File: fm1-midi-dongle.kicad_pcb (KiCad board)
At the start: 4 copper layers, 20 x 37.7 mm, 28 parts, among them J1 TYPE-C 24P-GTJB 040, J2 TYPE-C-31-M-12, J3 PJ-320D, J4 PJ-320D, U1 CH32X035G8U6, U2 XC6206P332MR, U3 SY6280AAC, U4 H11L1SM

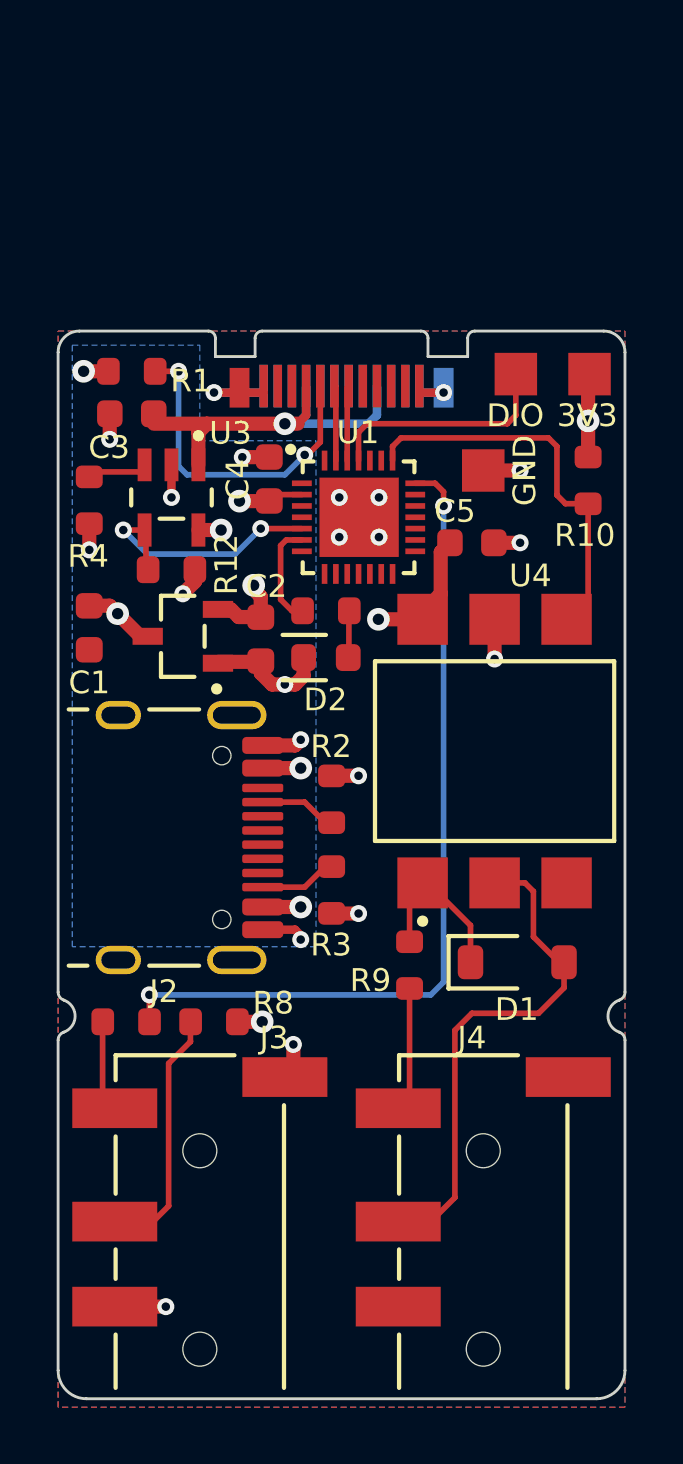
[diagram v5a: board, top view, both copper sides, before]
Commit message: Add hardware MIDI THRU: U5 SPDT switch selects OUT jack source
SN74LVC1G3157DCKR (LCSC C38663) in front of R7/J3 tip: S low = MIDI_RX
(opto output, hardware THRU), S high = MIDI_TX. S = OUT_SEL = PB9 with
R13 100k pull-down so THRU is the default with a blank or resetting MCU.

Layout: U5 between MCU and opto, C5 and R13 moved, TP3 (GND) moved to
the pocket above the jacks. ERC 0, DRC only the 6 known J1 edge items.
BOM, DESIGN.md and renders updated; SC-70-6 STEP vendored.

Co-Authored-By: Claude Opus 5.5 <noreply@anthropic.com>
Claude-Session: https://claude.ai/code/session_01Dtfv3zuhZTs975LiSXznFQ
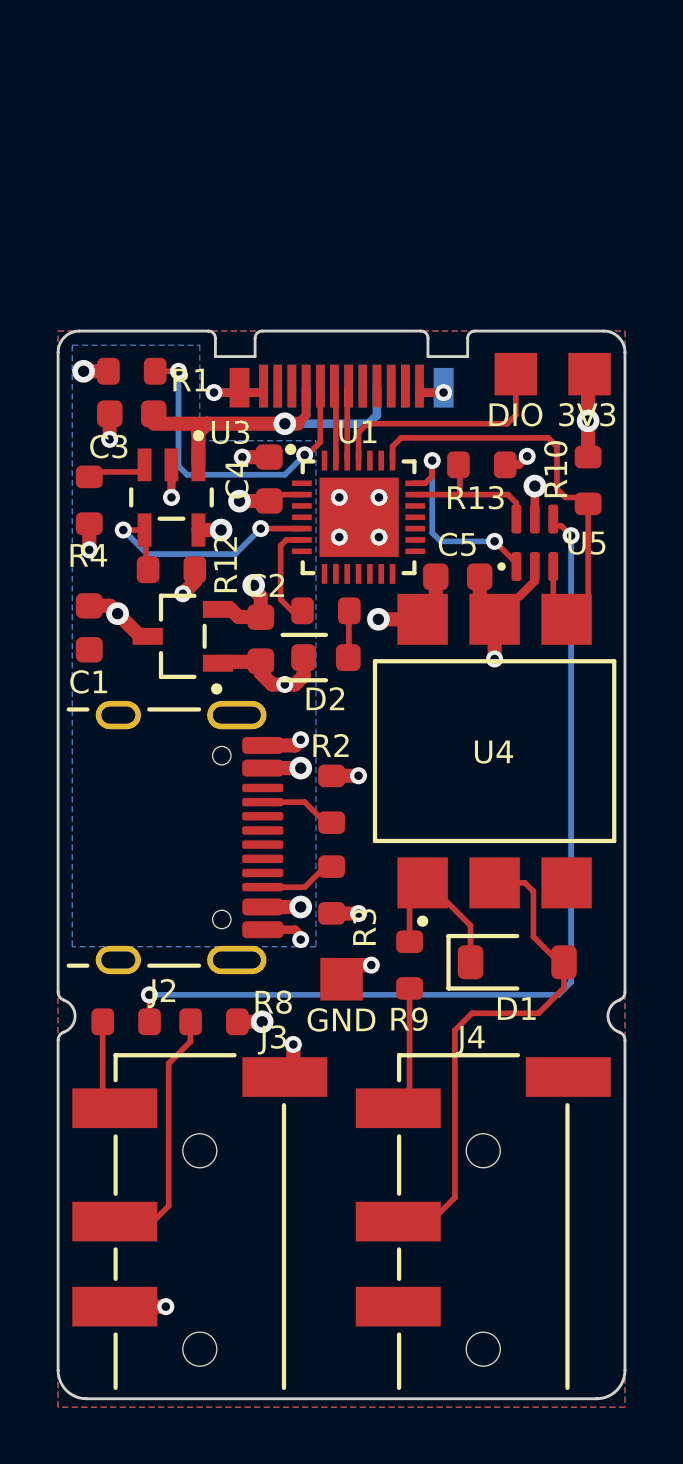
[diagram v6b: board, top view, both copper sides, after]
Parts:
- added R13: 100k, R_0603_1608Metric, F.Cu at (4.95, 2.75)
- added U5: SN74LVC1G3157, SOT-363_SC-70-6, F.Cu at (6.82, 5.50)
- moved TP3 18.6 mm to (0.00, 20.9)
- moved C5 1.30 mm to (4.10, 6.70)
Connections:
- R7 pad 1: /MIDI_TX -> /MIDI_OUT_DATA
- U1 pad 20: (no net) -> /OUT_SEL
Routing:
- net /MIDI_OUT_DATA: track 0.00 -> 32.5 mm, vias 0 -> 2
- net /MIDI_TX: track 29.9 -> 7.08 mm
- net /OUT_SEL: track 0.00 -> 4.57 mm
- net +3V3: track 13.1 -> 11.8 mm, vias 5 -> 6
- net GND: track 26.1 -> 27.0 mm

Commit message: v5: USB-A host port on the bottom face, schematic cleanup, hand-routed
- J1 = USB-A receptacle 911-321B2028S10100 (LCSC C42474) on B.Cu, mouth 0.8 mm
  past the top edge; board still 20 x 37.7 mm. Plug, R1 and CC_FM1 removed,
  VBUS_HOST, C3 now 10 uF (C96446) host-port bulk.
- Schematic: power/ground as KiCad power symbols, no overlapping symbols or
  texts (generator checks it), clean symbols for SY6280, 3157, USB-A, PJ-320D.
- THRU switch inputs swapped (B2 = MIDI_RX, B1 = MIDI_TX) and R13 is now a
  pull-up: THRU still default; firmware drives PB9 low for MCU MIDI.
- Floorplan + hand-written routing (tools/route.py): DRC 0 unconnected, house
  style clean, 0 loops. One track_width neck at U1 VDD (0.4 mm pitch).
- TP3 (GND) moved to the top-left corner; opto block 2.1 mm lower.
- Renders, BOM and DESIGN.md updated.

Co-Authored-By: Claude Opus 5.5 <noreply@anthropic.com>
Claude-Session: https://claude.ai/code/session_01Dtfv3zuhZTs975LiSXznFQ
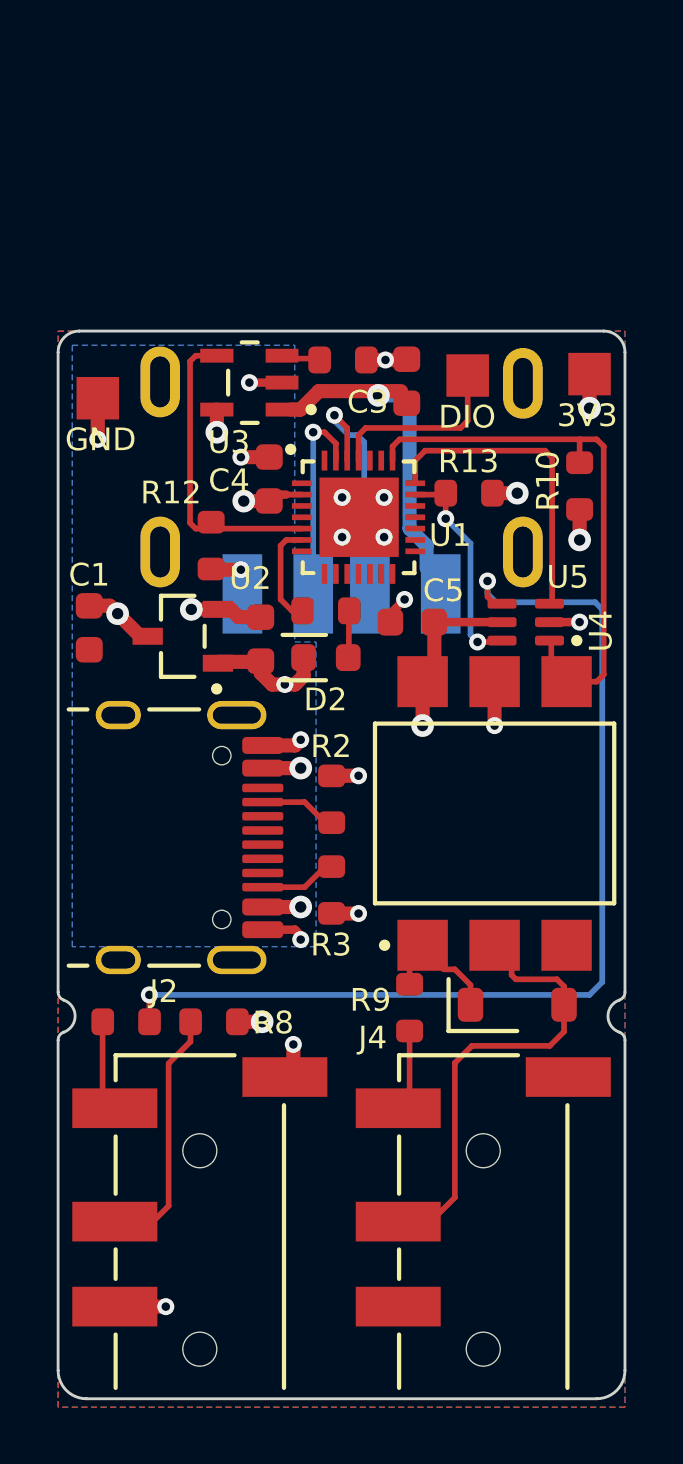
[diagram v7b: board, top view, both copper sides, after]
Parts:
- removed R1: 56k, R_0603_1608Metric
- C3: value 1u -> 10u
- J1: value TYPE-C 24P-GTJB 040 -> 911-321B2028S10100; footprint USB-C-SMD_TYPE-C-24P-GTJB-040 -> USB-A-SMD_911-321B2028S10100; moved to B.Cu
- moved TP3 22.2 mm to (-8.60, 0.40)
- moved R4 10.2 mm to (0.05, -0.95), turned to 0 degrees
- moved C3 9.77 mm to (2.30, -0.20), turned to 90 degrees
- moved U3 4.90 mm to (-3.25, -0.15), turned to 90 degrees
- moved J1 3.56 mm to (0.00, 3.56), turned to 0 degrees
- moved U5 2.82 mm to (6.50, 8.30), turned to 180 degrees
- moved C5 2.26 mm to (2.50, 8.30), turned to 180 degrees
- moved U4 2.20 mm to (5.40, 15.1)
- moved TP2 1.70 mm to (4.45, -0.40)
- moved R12 1.64 mm to (-4.60, 5.60), turned to -90 degrees
- moved D1 1.50 mm to (6.20, 21.8)
- moved R9 1.50 mm to (2.40, 21.9)
- moved R13 1.10 mm to (4.50, 3.75), turned to 180 degrees
- moved R10 0.36 mm to (8.40, 3.50), turned to 90 degrees
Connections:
- C3 pad 1: /VBUS_FM1 -> VBUS_HOST
- R13 pad 1: /OUT_SEL -> +3V3
- R13 pad 2: GND -> /OUT_SEL
- U3 pad 1: /VBUS_FM1 -> VBUS_HOST
- U5 pad 1: /MIDI_TX -> /MIDI_RX
- U5 pad 3: /MIDI_RX -> /MIDI_TX
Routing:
- net /VBUS_FM1: track 13.9 -> 0.00 mm, vias 1 -> 0
- net /CC_FM1: track 11.7 -> 0.00 mm, vias 2 -> 0
- net VBUS_HOST: track 0.00 -> 11.4 mm, vias 0 -> 1
- net GND: track 27.0 -> 20.5 mm, vias 21 -> 19
- net /USB_DM: track 2.60 -> 7.80 mm, vias 0 -> 1
- net /MIDI_RX: track 13.4 -> 18.2 mm
- net /MIDI_TX: track 7.08 -> 11.0 mm, vias 2 -> 0
- net /USB_DP: track 2.60 -> 6.37 mm, vias 0 -> 1
- net /MIDI_IN_RING: track 18.2 -> 14.6 mm
- net /MIDI_OUT_DATA: track 32.5 -> 35.9 mm
- net /OUT_SEL: track 4.57 -> 7.34 mm, vias 0 -> 2
- net /OPTO_A: track 4.28 -> 1.98 mm
- net /SDI_DIO: track 8.25 -> 5.96 mm
- net /VBUS_EN: track 8.77 -> 10.6 mm, vias 2 -> 0
- net /MIDI_IN_TIP: track 4.22 -> 2.57 mm
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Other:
- outline, holes or cut-outs redrawn
- board text added: "USB HOST"
- board text added: "v5 2026-10"
- board text removed: "v4 2026-10"

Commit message: v6: flat-slab layout, hand-routed, slab case
Owner rejected the v5 S-profile case (can't lie flat on a desk) and chose a
re-placed board in a uniform 12.2 mm slab.

- Board (still 20 x 37.7 mm): tall parts on top (USB-A J1 now on top, USB-C
  J2 on the right edge, jacks, opto, THRU switch, LED); parts <= 1.3 mm on
  the bottom (MCU, LDO, SY6280, caps, SDI pads).
- Pins: VBUS_EN -> PA3 (pin 8), LED -> PB12 (pin 23); U5 B1 = RX, B2 = TX,
  R13 back to a pull-down (PB9 HIGH = MCU TX, default hardware THRU).
- Routing (tools/route.py, hand-written polylines): +5V_IN as an island in
  In2; DRC 0 unconnected / 0 clearance, 0 loops, style clean. Open for
  owner sign-off: VDD 0.2 mm neck, one 0.6/0.3 +5V via, 0.8 mm designators.
- tools/silk.py is face-aware (outlines, designators and labels on each
  part's own face, back text mirrored); per-face net renders.
- case/: rounded slab 22.8 x 41.0 x 12.2 mm, flat top and bottom, snap fit,
  USB-A / USB-C dishes, flush jacks, LED light pipe; check_fit 0 collisions.
- DESIGN.md v6 section and firmware pin changes; BOM notes.

Co-Authored-By: Claude Opus 5.5 <noreply@anthropic.com>
Claude-Session: https://claude.ai/code/session_01Dtfv3zuhZTs975LiSXznFQ
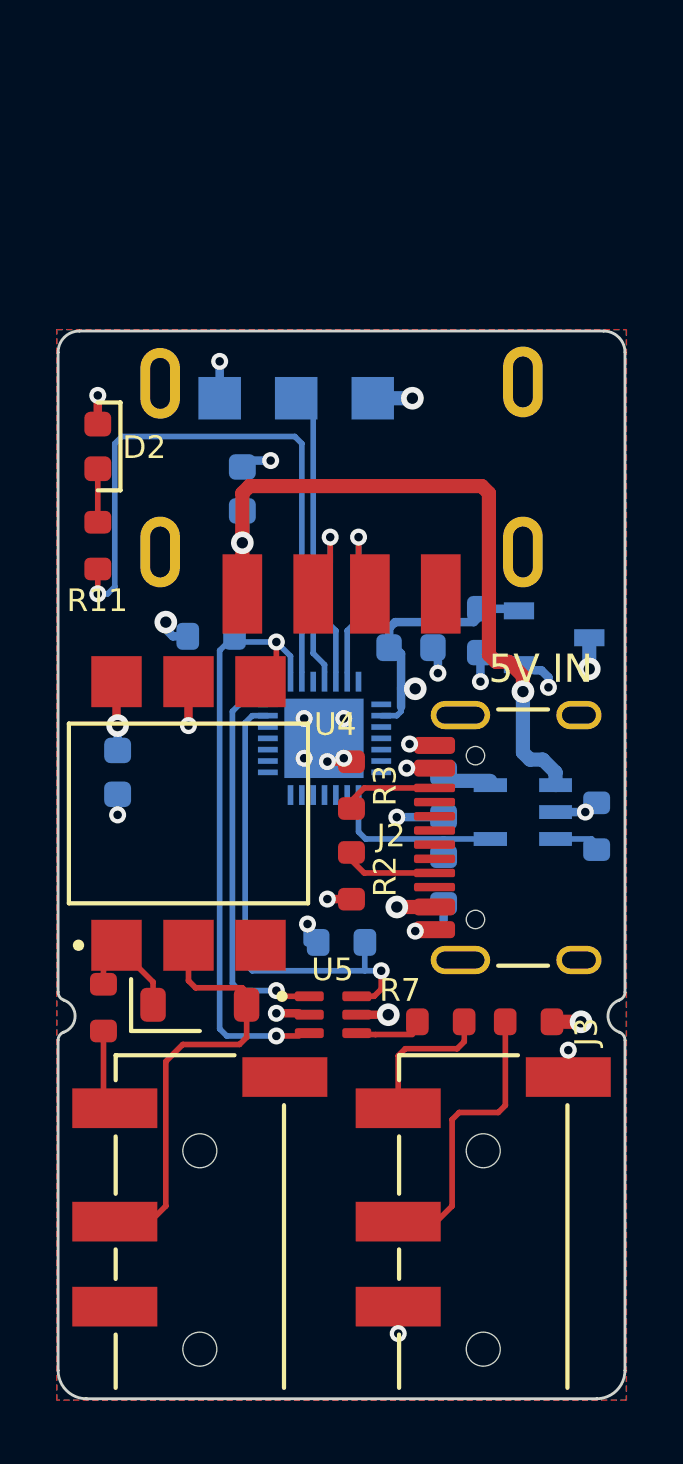
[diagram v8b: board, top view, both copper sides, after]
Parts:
- C1, C2, C3, C4, C5, R10, R12, R13, R4, TP1, TP2, TP3, U1, U2, U3: moved to B.Cu
- J1: moved to F.Cu
- moved R4 18.7 mm to (9.00, 15.5), turned to 90 degrees
- moved U3 18.0 mm to (6.40, 15.0), turned to -90 degrees
- moved R13 16.5 mm to (0.00, 19.6)
- moved U5 15.4 mm to (-0.30, 22.1), turned to 0 degrees
- moved R12 14.4 mm to (3.60, 17.4)
- moved J2 14.2 mm to (7.33, 15.9), turned to 90 degrees
- moved R10 14.0 mm to (-4.60, 8.80), turned to 0 degrees
- moved C1 13.8 mm to (3.60, 14.4)
- moved U2 13.1 mm to (7.50, 8.85), turned to 180 degrees
- moved C5 11.7 mm to (-7.90, 13.6), turned to -90 degrees
- moved D1 11.2 mm to (-5.00, 21.8)
- moved R7 11.1 mm to (3.50, 22.4), turned to 0 degrees
- moved R8 11.1 mm to (6.60, 22.4)
- moved D2 11.0 mm to (-8.60, 2.10), turned to -90 degrees
- moved R9 10.8 mm to (-8.40, 21.9)
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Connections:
- R13 pad 1: +3V3 -> /OUT_SEL
- R13 pad 2: /OUT_SEL -> GND
- U1 pad 23: (no net) -> /LED
- U1 pad 5: /VBUS_EN -> (no net)
- U1 pad 6: /LED -> (no net)
- U1 pad 8: (no net) -> /VBUS_EN
- U5 pad 1: /MIDI_RX -> /MIDI_TX
- U5 pad 3: /MIDI_TX -> /MIDI_RX
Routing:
- net /MIDI_OUT_DATA: track 35.9 -> 1.60 mm, vias 2 -> 0
- net /LED: track 3.67 -> 21.5 mm, vias 0 -> 1
- net VBUS_HOST: track 11.4 -> 24.3 mm, vias 1 -> 2
- net /OUT_SEL: track 7.34 -> 16.6 mm, vias 2 -> 1
- net GND: track 20.5 -> 13.0 mm, vias 19 -> 22
- net /VBUS_EN: track 10.6 -> 6.32 mm
- net /SDI_DIO: track 5.96 -> 9.62 mm
- net +3V3: track 12.5 -> 15.2 mm, vias 7 -> 6
- net /MIDI_TX: track 11.0 -> 13.5 mm, vias 0 -> 1
- net /USB_DM: track 7.80 -> 5.73 mm
- net /MIDI_TIP_OUT: track 3.05 -> 4.94 mm
- net /MIDI_RX: track 18.2 -> 19.9 mm, vias 0 -> 2
- net +5V_IN: track 5.99 -> 4.70 mm, vias 4 -> 3
- net /MIDI_RING_OUT: track 8.95 -> 10.2 mm
- net /OPTO_A: track 1.98 -> 2.88 mm
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- added copper zone on In2.Cu, net +5V_IN
- removed copper zone on B.Cu, net +5V_IN
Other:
- board text added: "v6 2026-10"
- board text removed: "v5 2026-10"
